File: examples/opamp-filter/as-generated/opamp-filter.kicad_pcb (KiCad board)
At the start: 2 copper layers, 80 x 45 mm, 17 parts, among them J1 IN, J2 5V, J3 OUT, U1 MCP6001R, U2 MCP6001R

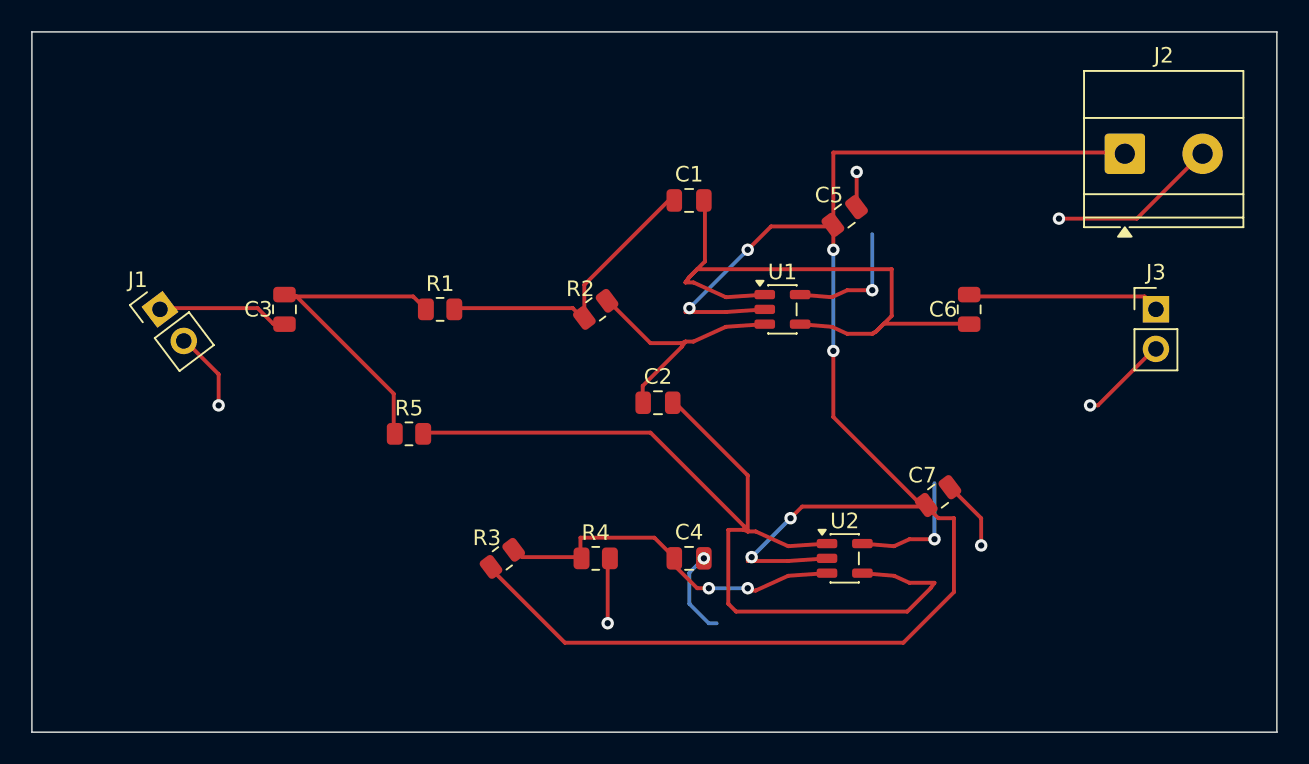
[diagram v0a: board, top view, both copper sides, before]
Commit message: Finish the fifth example, and stamp the model that wrote them
All five reviewed boards now pass KiCad's own checks: no DRC errors, nothing
unconnected, no schematic-parity findings, on 9.0.9 and 10.0.4. What is left
across the whole set is four silkscreen warnings and one library-footprint
hash, all of which come from the KiCad footprints themselves.

Getting the iCE40 board there found five things, each of which was silently
producing a board that was not the board the schematic described:

* **Two nets touching on the sheet is not something an endpoint check can
  see.** A wire that ends *on* another wire joins them, and on a sheet where
  every pin drags a stub behind it that is the common case. `schematic_shorts`
  looks for it now, and found three on this design - one of which had merged
  the 1.2 V and 3.3 V rails. The only visible sign had been KiCad's parity
  check disagreeing about a net name.
* **A symbol drawn in four units has to be placed four times.** Emitting all
  forty-eight pins under `(unit 1)` leaves three quarters of them in units
  that were never placed, which is twenty-five parity findings and a sheet
  nobody can read. The iCE40's banks and its supplies are four boxes now.
* **A pin the design does not use still has a net.** KiCad names it
  `unconnected-(U1A-IOT_37a-Pad23)`; a board that leaves the pad bare disagrees
  about every one of them.
* **A QFN counts anticlockwise**, so its east and north rows run bottom-to-top
  and right-to-left, and handing them to the fan-out in number order made
  every escape on those sides cross every other one.
* **Two rectangles that meet at a corner are further apart than growing both
  and asking whether they intersect makes them look** - which is every pair of
  pads on the corner of a QFN.

And two smaller ones: the router now keeps its vias away from every drilled
hole rather than only from its own, and the degraded variant is degraded from
the *routed* design rather than re-routed, which is both th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
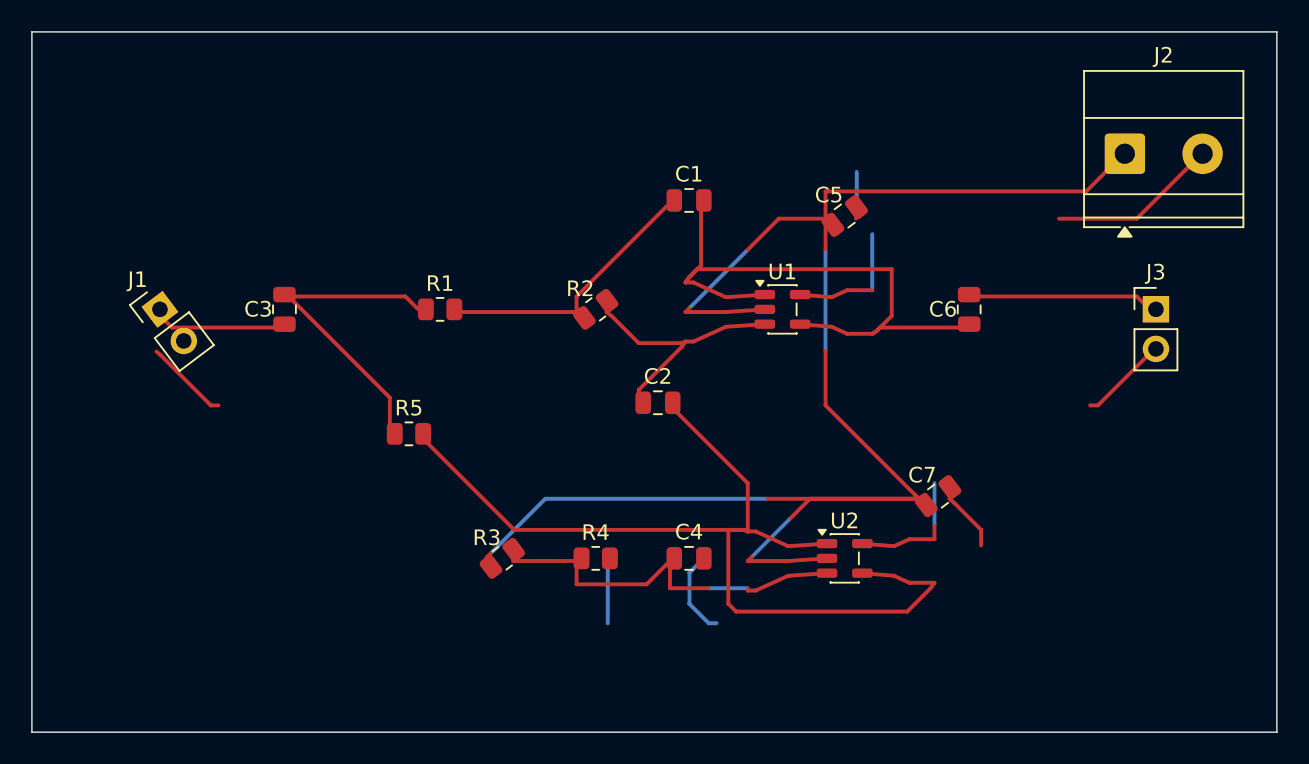
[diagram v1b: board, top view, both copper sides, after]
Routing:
- net +5V: track 119.1 -> 106.3 mm, vias 6 -> 0
- net /X: track 18.8 -> 17.7 mm
- net /MID: track 23.7 -> 24.6 mm, vias 2 -> 0
- net GND: track 55.1 -> 54.4 mm, vias 9 -> 0
- net /OUT: track 40.6 -> 40.0 mm

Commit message: Read the five as an engineer would, and make the toolkit act on it
examples/REVIEW.md is the pass: the five designs read for circuit theory,
layout physics and readability, every finding dispatched to one of four
places - a rule, a fix, a reasoned waiver, or named as open. The headline
result: every reviewed/ project now PASSES its own gate, every as-generated/
still fails it, and every waiver is an engineering argument a reviewer can
disagree with.

Four new rules, each calibrated against KiCad's 18 human-drawn demo projects:

* readability.label_only - the sheet connects by name, not by wire; the
  single most recognisable mark of a generated schematic. 0 findings on the
  human corpus, 71-100% on ours.
* analog.no_dc_path - a net of only capacitors and connectors has nothing
  setting its DC level. Found a real fault: the op-amp filter's AC-coupled
  output floated. 0 findings on the corpus.
* route.detour - routed copper against the MST of the net's pads; the scenic
  tour an autorouter takes. 8 human boards fired at 2.5x, 0 at the shipped 4x.
* route.return_path - signal running over cuts in the other layer's ground
  fill, computed from the difference between a zone's outline and its fill,
  which the parser now keeps. Fires on 4 real demo boards, because real
  two-layer boards genuinely have the disease.

Three rules re-judged on evidence instead of names:

* analog.missing_decoupling reads pin electrical types: only power_in pins
  ask for a capacitor, and a net an output pin drives is never asked - a cap
  on an op-amp output is somebody's control loop. Retires the VBUS/VREF
  false positives without a single waiver.
* track.thin_power measures the longest contiguous narrow run against a
  power_neck_mm allowance. Pad entries and fine-pitch escapes pass; thin
  trunks still fail. 9 demo boards fired before, 0 after - all nine were necks.
* net.single_pin honours no-connect flags: a flagged pin is a decision.

And the designs themselves got the fixes the pa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
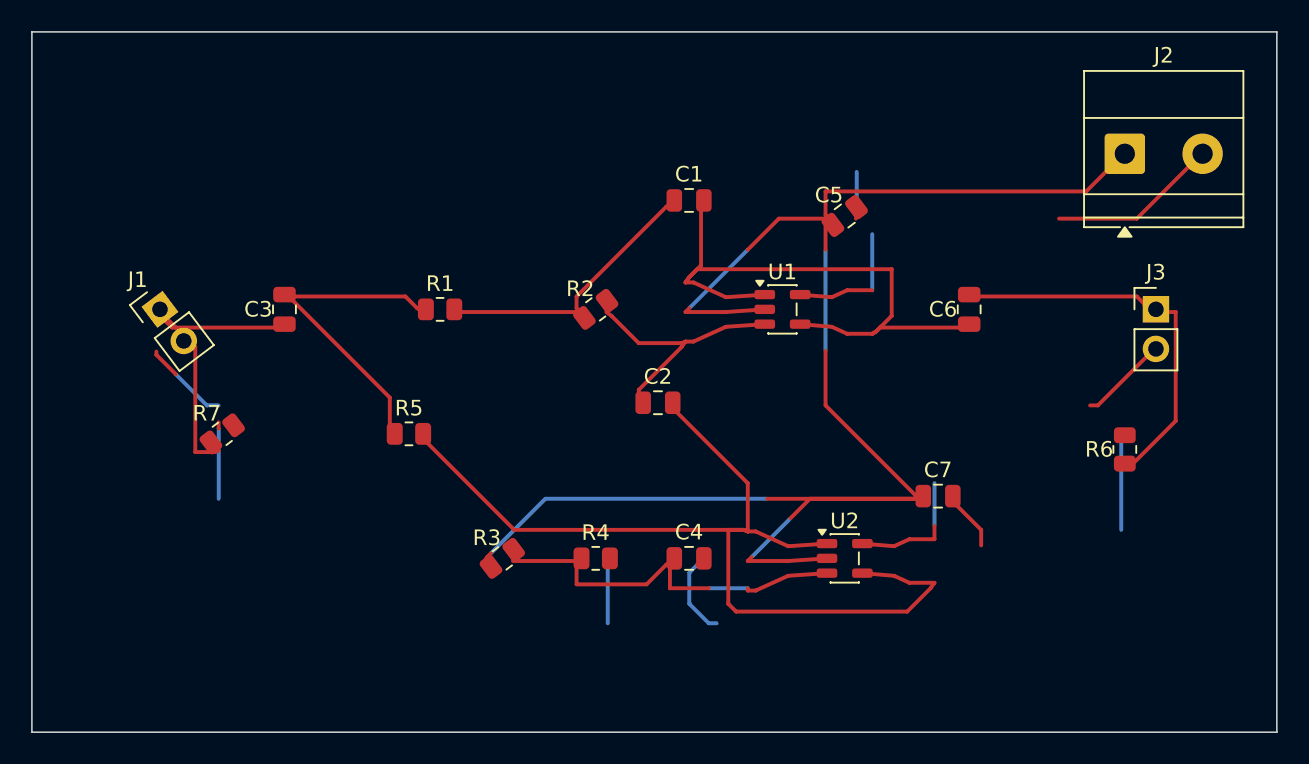
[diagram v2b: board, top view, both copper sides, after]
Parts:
- added R6: 100k, Resistor_SMD:R_0805_2012Metric, F.Cu at (170.2, 86.8)
- added R7: 100k, Resistor_SMD:R_0805_2012Metric, F.Cu at (112.2, 85.8)
- turned C7 to 0 degrees
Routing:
- net /OUT_AC: track 12.4 -> 25.7 mm
- net /IN: track 8.42 -> 20.1 mm
- net GND: track 54.4 -> 65.3 mm
